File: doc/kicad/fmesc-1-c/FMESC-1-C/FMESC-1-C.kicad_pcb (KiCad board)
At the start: 2 copper layers, 48 x 48 mm, 118 parts, among them Q1 AON6504, Q10 AON6504, Q11 AON6504, Q12 AON6504, Q13 AON6504, Q14 AON6504, Q15 AON6504, Q16 AON6504, Q17 AON6504, Q18 AON6504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

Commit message: doc/kicad: FMESC-1-C add PCB
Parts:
- removed C10, C11, C12, C13, C20, C21, C22, C23, C30, C31, C32, C33, C40, C41, C42, C43: 10u, Capacitor_SMD:C_1206_3216Metric
- removed D11, D12, D13, D21, D22, D23, D31, D32, D33, D41, D42, D43: D, Diode_SMD:D_SMA
- removed JB0: Conn_01x01, fmlibf:JS3x10mm
- removed JB1, JB10, JB11, JB12, JB2, JB3, JB4, JB5, JB6, JB7, JB8, JB9: Conn_01x01, fmlibf:JS3x5mm
- removed JG0: Conn_01x01, fmlibf:JS4x16mm
- removed JG1, JG10, JG11, JG12, JG2, JG3, JG4, JG5, JG6, JG7, JG8, JG9, MA1, MA2, MA3, MA4, MB1, MB2, MB3, MB4, MC1, MC2, MC3, MC4: Conn_01x01, fmlibf:JS3x4mm
- removed Q1, Q10, Q11, Q12, Q13, Q14, Q15, Q16, Q17, Q18, Q19, Q2, Q20, Q21, Q22, Q23, Q24, Q3, Q4, Q5, Q6, Q7, Q8, Q9: AON6504, fmlibf:DFN5x6_8L_EP1_P
- removed R11, R12, R13, R14, R15, R16, R21, R22, R23, R24, R25, R26, R31, R32, R33, R34, R35, R36, R41, R42, R43, R44, R45, R46: 10, Resistor_SMD:R_0402_1005Metric
- removed U2, U3, U4: FD6288Q, Package_DFN_QFN:QFN-24-1EP_4x4mm_P0.5mm_EP2.7x2.7mm
- added C0: 10u, Capacitor_SMD:C_1206_3216Metric, B.Cu at (133.0, 63.0)
- added C1: 10u, Capacitor_SMD:C_1206_3216Metric, F.Cu at (125.0, 71.5)
- added C2: 10u, Capacitor_SMD:C_1206_3216Metric, F.Cu at (125.0, 66.0)
- added C3: 10u, Capacitor_SMD:C_1206_3216Metric, F.Cu at (125.0, 60.5)
- added D1: D, Diode_SMD:D_SMA, F.Cu at (120.0, 71.0)
- added D2: D, Diode_SMD:D_SMA, F.Cu at (120.0, 65.5)
- added D3: D, Diode_SMD:D_SMA, F.Cu at (120.0, 60.0)
- added J1: Conn_01x02, fmlibf:JT_2P_1.0mm, F.Cu at (122.5, 68.5)
- added J2: Conn_01x02, fmlibf:JT_2P_1.0mm, F.Cu at (117.5, 68.5)
- added J3: Conn_01x02, fmlibf:JT_2P_1.0mm, F.Cu at (122.5, 63.0)
- added J4: Conn_01x02, fmlibf:JT_2P_1.0mm, F.Cu at (117.5, 63.0)
- added J5: Conn_01x02, fmlibf:JT_2P_1.0mm, F.Cu at (122.5, 57.5)
- added J6: Conn_01x02, fmlibf:JT_2P_1.0mm, F.Cu at (117.5, 57.5)
- added JC1: Conn_01x12, fmlibf:JS_12P_1.0mm, F.Cu at (115.0, 64.5)
- added JP1: Conn_01x02, fmlibf:JT_2P_1.0mm, F.Cu at (117.5, 73.5)
- added R1: 10, Resistor_SMD:R_0402_1005Metric, B.Cu at (122.5, 70.0)
- added R2: 10, Resistor_SMD:R_0402_1005Metric, B.Cu at (117.5, 70.0)
- added R3: 10, Resistor_SMD:R_0402_1005Metric, B.Cu at (122.5, 64.5)
- added R4: 10, Resistor_SMD:R_0402_1005Metric, B.Cu at (117.5, 64.5)
- added R5: 10, Resistor_SMD:R_0402_1005Metric, B.Cu at (122.5, 59.0)
- added R6: 10, Resistor_SMD:R_0402_1005Metric, B.Cu at (117.5, 59.0)
- moved U1 54.3 mm to (131.0, 67.0), turned to 270 degrees
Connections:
- U1 pad 1: /M1/CAL1 -> /CAL1
- U1 pad 10: /M1/BLG -> /BLG
- U1 pad 11: /M1/ALG -> /ALG
- U1 pad 12: /M1/C1 -> /C1
- U1 pad 13: /M1/CHG -> /CHG
- U1 pad 15: /M1/B1 -> /B1
- U1 pad 16: /M1/BHG -> /BHG
- U1 pad 18: /M1/A1 -> /A1
- U1 pad 19: /M1/AHG -> /AHG
- U1 pad 2: /M1/CBL1 -> /CBL1
- U1 pad 22: /M1/CAH1 -> /CAH1
- U1 pad 23: /M1/CBH1 -> /CBH1
- U1 pad 24: /M1/CCH1 -> /CCH1
- U1 pad 3: /M1/CCL1 -> /CCL1
- U1 pad 9: /M1/CLG -> /CLG
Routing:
- net +BATT: track 256.5 -> 0.00 mm, vias 9 -> 0
- net GND: track 171.0 -> 0.00 mm, vias 5 -> 0
- net /M1/ALG: track 35.5 -> 0.00 mm
- net /M1/BLG: track 27.2 -> 0.00 mm
- net /M2/C1: track 23.8 -> 0.00 mm, vias 2 -> 0
- net /M2/A1: track 23.8 -> 0.00 mm, vias 2 -> 0
- net /M2/B1: track 23.5 -> 0.00 mm, vias 2 -> 0
- net /M4/B1: track 23.3 -> 0.00 mm, vias 2 -> 0
- net /M3/C1: track 23.2 -> 0.00 mm, vias 2 -> 0
- net /M4/C1: track 23.1 -> 0.00 mm, vias 2 -> 0
- net /M4/A1: track 23.0 -> 0.00 mm, vias 2 -> 0
- net /M3/B1: track 23.0 -> 0.00 mm, vias 2 -> 0
- net /M3/A1: track 23.0 -> 0.00 mm, vias 2 -> 0
- net /M1/CLG: track 19.1 -> 0.00 mm
- net Net-(C1-Pad1): track 17.4 -> 0.00 mm, vias 1 -> 0
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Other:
- board size 48 x 48 mm -> 13 x 21 mm

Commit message: doc/kicad: FMESC-1-C PCB layout
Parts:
- added JC2: Conn_01x04, fmlibf:JS_4P_1.0mm, F.Cu at (115.0, 64.5)
- added JC3: Conn_01x04, fmlibf:JS_4P_1.0mm, F.Cu at (115.0, 71.0)
- JC1: value Conn_01x12 -> Conn_01x04; footprint fmlibf:JS_12P_1.0mm -> fmlibf:JS_4P_1.0mm
- moved C0 11.5 mm to (122.0, 59.5)
- moved U1 11.1 mm to (120.5, 63.5)
- moved JC1 6.00 mm to (115.0, 58.5), turned to 270 degrees
- moved J5 3.91 mm to (125.0, 54.5), turned to 180 degrees
- moved R6 3.61 mm to (115.5, 56.0), turned to 90 degrees
- moved R5 3.60 mm to (124.5, 56.0), turned to 90 degrees
- moved J6 3.35 mm to (116.0, 54.5), turned to 180 degrees
- moved C3 3.00 mm to (125.0, 57.5)
- moved D3 3.00 mm to (120.0, 57.0)
- moved J3 2.92 mm to (125.0, 61.5), turned to 180 degrees
- moved J1 2.50 mm to (125.0, 68.5), turned to 180 degrees
- moved R3 2.50 mm to (124.5, 63.0), turned to 90 degrees
- moved R4 2.50 mm to (115.5, 63.0), turned to 90 degrees
- moved J4 2.12 mm to (116.0, 61.5), turned to 180 degrees
- moved R1 2.00 mm to (124.5, 70.0), turned to 90 degrees
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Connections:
- JC1 pad 1: /CAL1 -> GND
- JC1 pad 2: /CBL1 -> /CAL1
- JC1 pad 3: /CCL1 -> /CBL1
- JC1 pad 4: /CAH1 -> /CCL1

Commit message: doc/kicad: FMESC-1-C PCB v0.1
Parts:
- D1, D2, D3: footprint Diode_SMD:D_SMA -> Diode_SMD:D_0603_1608Metric
- moved C2 8.51 mm to (119.5, 58.0), turned to 180 degrees
- moved C0 6.71 mm to (125.0, 65.5), turned to 90 degrees
- moved C1 6.50 mm to (118.5, 71.5)
- moved C3 5.85 mm to (119.5, 55.5), turned to 180 degrees
- moved D2 5.59 mm to (122.5, 59.0), turned to 90 degrees
- moved R2 3.00 mm to (115.5, 67.0), turned to 270 degrees
- moved D3 2.69 mm to (122.5, 56.0), turned to 270 degrees
- moved D1 2.06 mm to (120.5, 73.0), turned to 270 degrees
- moved U1 1.58 mm to (120.0, 65.0)
- moved R1 0.71 mm to (124.0, 69.5), turned to 0 degrees
- moved R3 0.71 mm to (124.0, 62.5), turned to 0 degrees
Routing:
- net GND: track 0.00 -> 51.9 mm, vias 0 -> 3
- net +BATT: track 0.00 -> 35.4 mm, vias 0 -> 2
- net /C1: track 0.00 -> 26.2 mm, vias 0 -> 2
- net /B1: track 0.00 -> 21.2 mm, vias 0 -> 3
- net /CHG: track 0.00 -> 16.5 mm, vias 0 -> 2
- net Net-(C2-Pad1): track 0.00 -> 16.4 mm, vias 0 -> 1
- net Net-(C3-Pad1): track 0.00 -> 16.0 mm, vias 0 -> 3
- net Net-(C1-Pad1): track 0.00 -> 12.0 mm, vias 0 -> 1
- net /CLG: track 0.00 -> 9.62 mm, vias 0 -> 2
- net /A1: track 0.00 -> 8.83 mm, vias 0 -> 1
- net /BHG: track 0.00 -> 8.06 mm, vias 0 -> 2
- net /CAL1: track 0.00 -> 7.47 mm, vias 0 -> 1
- net /CBL1: track 0.00 -> 7.44 mm, vias 0 -> 1
- net /CCL1: track 0.00 -> 6.57 mm, vias 0 -> 1
- net /CCH1: track 0.00 -> 4.92 mm, vias 0 -> 1
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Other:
- board text added: "2020-11-09"
- board text added: "FMESC-1-C v0.1"

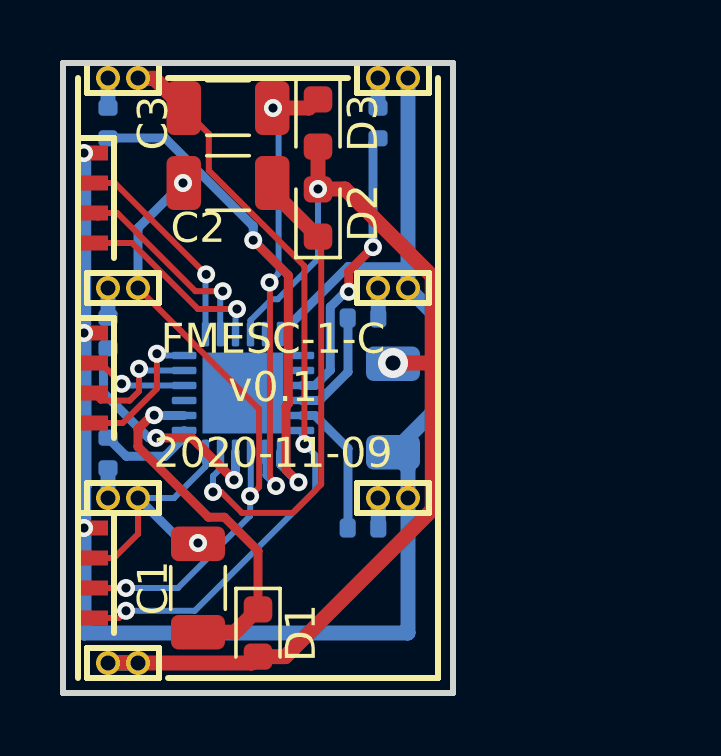
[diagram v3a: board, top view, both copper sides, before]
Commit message: doc/kicad: FMESC-1-C update sch and clean
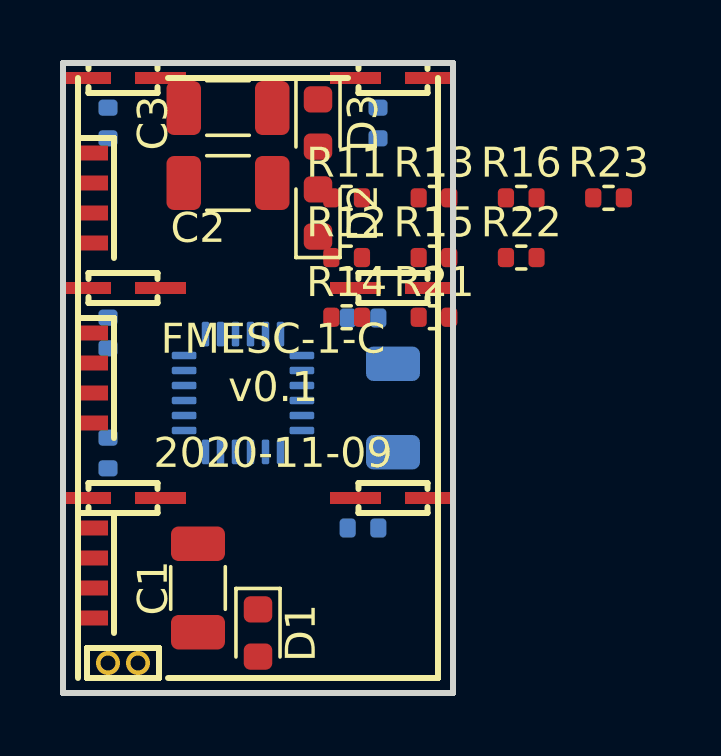
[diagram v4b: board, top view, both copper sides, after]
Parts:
- added R11: 2k, Resistor_SMD:R_0402_1005Metric, F.Cu at (123.5, 58.5)
- added R12: 20k, Resistor_SMD:R_0402_1005Metric, F.Cu at (123.5, 60.5)
- added R13: 2k, Resistor_SMD:R_0402_1005Metric, F.Cu at (126.4, 58.5)
- added R14: 20k, Resistor_SMD:R_0402_1005Metric, F.Cu at (123.5, 62.5)
- added R15: 2k, Resistor_SMD:R_0402_1005Metric, F.Cu at (126.4, 60.5)
- added R16: 20k, Resistor_SMD:R_0402_1005Metric, F.Cu at (129.3, 58.5)
- added R21: 2k, Resistor_SMD:R_0402_1005Metric, F.Cu at (126.4, 62.5)
- added R22: 2k, Resistor_SMD:R_0402_1005Metric, F.Cu at (129.3, 60.5)
- added R23: 2k, Resistor_SMD:R_0402_1005Metric, F.Cu at (132.2, 58.5)
- J1, J2, J3, J4, J5, J6: footprint fmlibf:JT_2P_1.0mm -> fmlibf:JS_2P_1.0mm_2
- U1: footprint Package_DFN_QFN:QFN-24-1EP_4x4mm_P0.5mm_EP2.7x2.7mm -> fmlibf:QFN-24-1EP_4x4mm_P0.5mm_EP2.7x2.7mm_nopad
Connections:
- JC3 pad 1: GND -> /S0
- JC3 pad 2: /A1 -> /SA
- JC3 pad 3: /B1 -> /SB
- JC3 pad 4: /C1 -> /SC
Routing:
- net GND: track 51.9 -> 0.00 mm, vias 3 -> 0
- net +BATT: track 35.4 -> 0.00 mm, vias 2 -> 0
- net /C1: track 26.2 -> 0.00 mm, vias 2 -> 0
- net /B1: track 21.2 -> 0.00 mm, vias 3 -> 0
- net /CHG: track 16.5 -> 0.00 mm, vias 2 -> 0
- net Net-(C2-Pad1): track 16.4 -> 0.00 mm, vias 1 -> 0
- net Net-(C3-Pad1): track 16.0 -> 0.00 mm, vias 3 -> 0
- net Net-(C1-Pad1): track 12.0 -> 0.00 mm, vias 1 -> 0
- net /CLG: track 9.62 -> 0.00 mm, vias 2 -> 0
- net /A1: track 8.83 -> 0.00 mm, vias 1 -> 0
- net /BHG: track 8.06 -> 0.00 mm, vias 2 -> 0
- net /CAL1: track 7.47 -> 0.00 mm, vias 1 -> 0
- net /CBL1: track 7.44 -> 0.00 mm, vias 1 -> 0
- net /CCL1: track 6.57 -> 0.00 mm, vias 1 -> 0
- net /CCH1: track 4.92 -> 0.00 mm, vias 1 -> 0
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
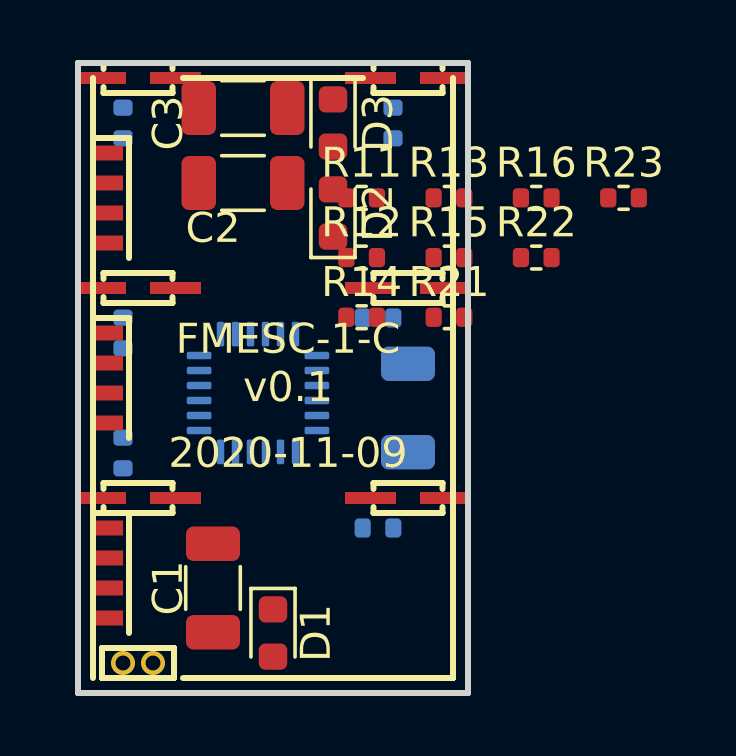
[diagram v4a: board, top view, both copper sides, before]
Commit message: doc/kicad: FMESC-1-C PCB wire fail (1)
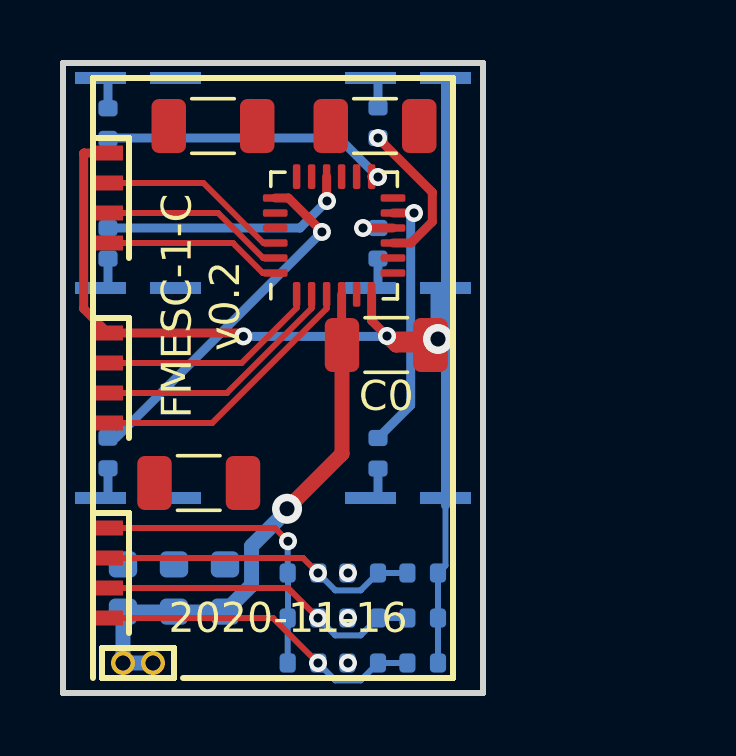
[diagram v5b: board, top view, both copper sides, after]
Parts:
- C0, U1: moved to F.Cu
- D1, D2, D3, J1, J2, J3, J4, J5, J6, R11, R12, R13, R14, R15, R16, R21, R22, R23: moved to B.Cu
- moved R23 18.8 mm to (121.5, 74.0)
- moved R16 16.5 mm to (123.5, 74.0), turned to 180 degrees
- moved D3 15.9 mm to (118.9, 71.5)
- moved R22 14.3 mm to (121.5, 72.5)
- moved R13 14.0 mm to (125.5, 72.5), turned to 180 degrees
- moved D2 13.6 mm to (117.2, 71.5), turned to 270 degrees
- moved R15 13.5 mm to (125.5, 74.0), turned to 180 degrees
- moved R11 12.7 mm to (125.5, 71.0), turned to 180 degrees
- moved R12 10.5 mm to (123.5, 71.0), turned to 180 degrees
- moved R14 10.0 mm to (123.5, 72.5), turned to 180 degrees
- moved R21 9.82 mm to (121.5, 71.0)
- moved JC1 6.00 mm to (115.0, 64.5)
- moved JC2 6.00 mm to (115.0, 58.5)
- moved U1 5.83 mm to (122.5, 59.8), turned to 90 degrees
- moved D1 5.22 mm to (115.5, 71.5)
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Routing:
- net GND: track 0.00 -> 42.0 mm, vias 0 -> 3
- net +BATT: track 0.00 -> 17.4 mm, vias 0 -> 1
- net /AHG: track 0.00 -> 11.7 mm, vias 0 -> 1
- net /SC: track 0.00 -> 11.1 mm, vias 0 -> 1
- net /SB: track 0.00 -> 10.9 mm, vias 0 -> 1
- net /SA: track 0.00 -> 10.7 mm, vias 0 -> 1
- net /S0: track 0.00 -> 10.3 mm, vias 0 -> 1
- net /CHG: track 0.00 -> 9.76 mm, vias 0 -> 1
- net /CCL1: track 0.00 -> 9.04 mm
- net /ALG: track 0.00 -> 8.70 mm, vias 0 -> 1
- net /BHG: track 0.00 -> 8.49 mm, vias 0 -> 1
- net /CBL1: track 0.00 -> 8.02 mm
- net /CAL1: track 0.00 -> 7.30 mm
- net /CAH1: track 0.00 -> 6.40 mm
- net /CBH1: track 0.00 -> 6.20 mm
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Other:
- board size 13 x 21 mm -> 14 x 21 mm
- board text added: "2020-11-16"
- board text added: "FMESC-1-C v0.2"
- board text removed: "2020-11-09"
- board text removed: "FMESC-1-C v0.1"

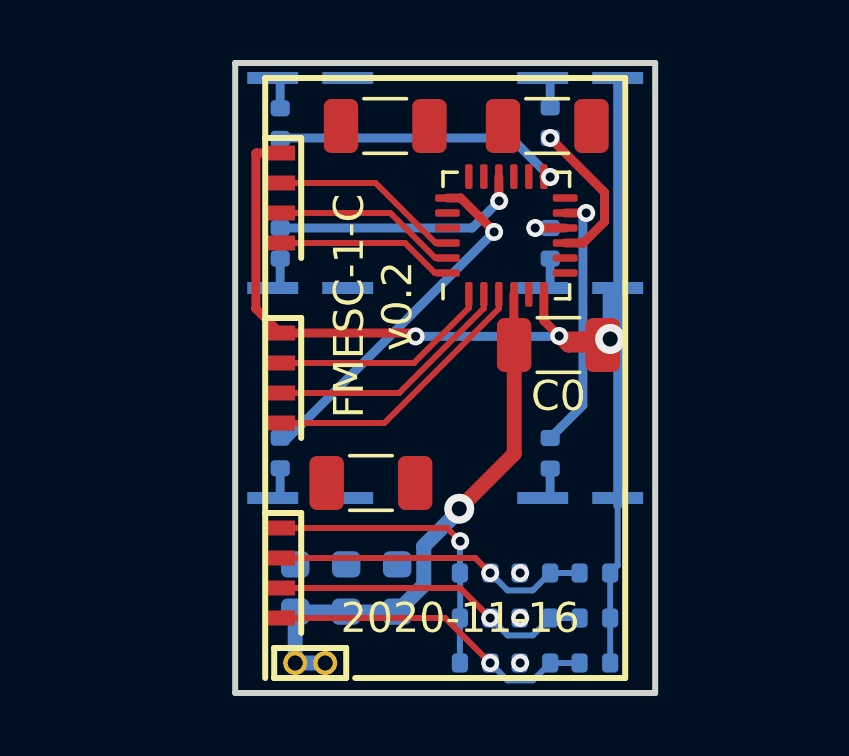
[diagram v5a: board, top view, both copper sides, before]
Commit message: doc/kicad: add fm02-b-1
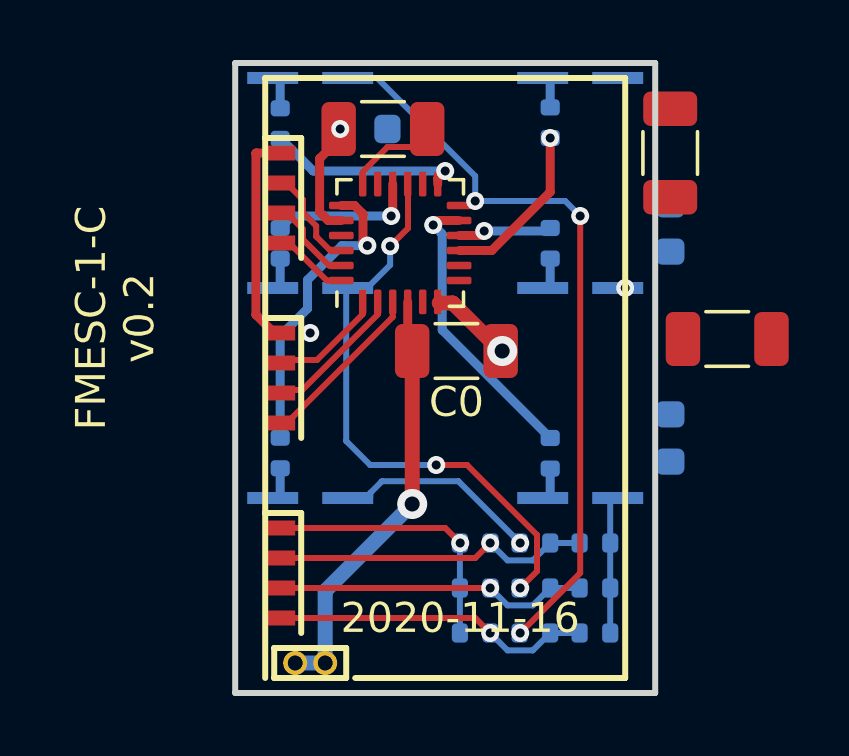
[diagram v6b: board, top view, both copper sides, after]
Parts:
- moved D1 15.5 mm to (117.8, 56.2), turned to 0 degrees
- moved D3 15.1 mm to (128.0, 59.5)
- moved C2 13.4 mm to (129.9, 63.2), turned to 180 degrees
- moved D2 11.9 mm to (128.0, 66.5)
- moved C1 11.8 mm to (118.4, 56.2)
- moved C3 4.20 mm to (128.0, 57.0), turned to 90 degrees
- moved U1 3.55 mm to (119.0, 60.0)
- moved C0 3.41 mm to (120.9, 63.6)
- moved R11 1.00 mm to (125.5, 70.0)
- moved R12 1.00 mm to (123.5, 70.0)
- moved R13 1.00 mm to (125.5, 71.5)
- moved R14 1.00 mm to (123.5, 71.5)
- moved R15 1.00 mm to (125.5, 73.0)
- moved R16 1.00 mm to (123.5, 73.0)
- moved R21 1.00 mm to (121.5, 70.0)
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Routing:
- net GND: track 42.0 -> 14.1 mm
- net /C1: track 0.00 -> 24.8 mm, vias 1 -> 3
- net /B1: track 0.00 -> 18.8 mm, vias 1 -> 3
- net /A1: track 0.00 -> 8.69 mm
- net /CAL1: track 7.30 -> 3.49 mm
- net /CCH1: track 5.89 -> 2.11 mm
- net /CCL1: track 9.04 -> 5.36 mm
- net /CBL1: track 8.02 -> 4.41 mm
- net /CBH1: track 6.20 -> 2.60 mm
- net /BHG: track 8.49 -> 4.95 mm
- net /CAH1: track 6.40 -> 3.09 mm
- net +BATT: track 17.4 -> 14.1 mm
- net /CHG: track 9.76 -> 6.50 mm
- net Net-(C1-Pad1): track 0.00 -> 3.17 mm, vias 0 -> 1
- net /AHG: track 11.7 -> 10.1 mm
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
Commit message: doc/kicad: FMESC-1-C PCB wire  almost finish
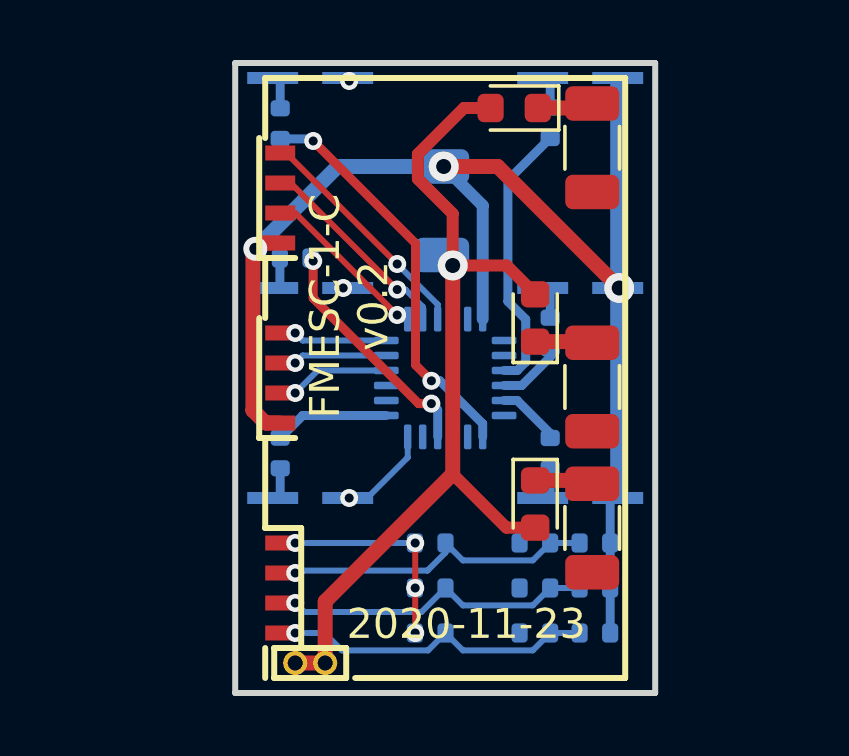
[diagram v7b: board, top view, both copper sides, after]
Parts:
- C0, U1: moved to B.Cu
- D1, D2, D3: moved to F.Cu
- moved C1 15.0 mm to (125.4, 69.5), turned to 270 degrees
- moved D1 13.7 mm to (123.5, 68.7), turned to 270 degrees
- moved D3 6.56 mm to (122.8, 55.5), turned to 180 degrees
- moved D2 6.02 mm to (123.5, 62.5), turned to 90 degrees
- moved JC1 6.00 mm to (115.0, 58.5), turned to 90 degrees
- moved JC2 6.00 mm to (115.0, 64.5), turned to 90 degrees
- moved C2 4.78 mm to (125.4, 64.8), turned to 270 degrees
- moved U1 4.74 mm to (120.5, 64.5), turned to 270 degrees
- moved C0 4.70 mm to (120.4, 58.9), turned to 270 degrees
- moved R3 2.99 mm to (124.0, 63.0), turned to 90 degrees
- moved C3 2.61 mm to (125.4, 56.8), turned to 270 degrees
- moved R21 1.50 mm to (120.0, 70.0)
- moved R22 1.50 mm to (120.0, 71.5)
- moved R23 1.50 mm to (120.0, 73.0)
- moved R4 0.70 mm to (115.5, 60.5), turned to 180 degrees
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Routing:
- net GND: track 14.1 -> 46.3 mm
- net /C1: track 24.8 -> 0.00 mm, vias 3 -> 1
- net /B1: track 18.8 -> 0.00 mm, vias 3 -> 1
- net +BATT: track 14.1 -> 31.7 mm
- net /ALG: track 9.50 -> 2.14 mm, vias 1 -> 0
- net /CHG: track 6.50 -> 13.5 mm, vias 1 -> 2
- net /AHG: track 10.1 -> 3.85 mm, vias 1 -> 0
- net /A1: track 8.69 -> 2.60 mm
- net /CLG: track 5.65 -> 9.14 mm, vias 1 -> 0
- net /BHG: track 4.95 -> 7.83 mm, vias 1 -> 2
- net /CCL1: track 5.36 -> 7.83 mm, vias 0 -> 1
- net /CBL1: track 4.41 -> 6.77 mm, vias 0 -> 1
- net /CAL1: track 3.49 -> 5.72 mm, vias 0 -> 1
- net /S0: track 9.22 -> 7.00 mm, vias 1 -> 4
- net Net-(C3-Pad1): track 0.00 -> 1.61 mm
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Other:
- board text added: "2020-11-23"
- board text removed: "2020-11-16"
